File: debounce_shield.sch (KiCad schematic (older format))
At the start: 54 parts, among them J1 Conn_01x06, J2 RPi_GPIO, J3 Conn_01x06, J4 Conn_01x06, J5 Conn_01x02, P2 CONN_2, U1 74LV14D, U2 CAT24C32, U3 LTV-824, U4 LTV-824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

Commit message: Change 6-position terminal to fixed Phoenix Contact 1990041 footprint.
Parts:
- J1, J3, J4: footprint GSL002C-2.50-06P:GSL002C25006P -> Phoenix_Contact_1990041:1990041
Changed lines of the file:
@@
 F 0 "J4" H 1500 5450 50  0000 C CNN
 F 1 "Conn_01x06" H 1500 5350 50  0000 C CNN
-F 2 "GSL002C-2.50-06P:GSL002C25006P" H 1500 5050 50  0001 C CNN
+F 2 "Phoenix_Contact_1990041:1990041" H 1500 5050 50  0001 C CNN
 F 3 "~" H 1500 5050 50  0001 C CNN
 F 4 "Phoenix Contact" H 1500 5050 50  0001 C CNN "Manufacturer_Name"
@@
 F 0 "J3" H 1418 3875 50  0000 C CNN
 F 1 "Conn_01x06" H 1418 3966 50  0000 C CNN
-F 2 "GSL002C-2.50-06P:GSL002C25006P" H 1500 4400 50  0001 C CNN
+F 2 "Phoenix_Contact_1990041:1990041" H 1500 4400 50  0001 C CNN
 F 3 "~" H 1500 4400 50  0001 C CNN
 F 4 "Phoenix Contact" H 1500 4400 50  0001 C CNN "Manufacturer_Name"
@@
 F 0 "J1" H 4018 1175 50  0000 C CNN
 F 1 "Conn_01x06" H 4018 1266 50  0000 C CNN
-F 2 "GSL002C-2.50-06P:GSL002C25006P" H 4100 1700 50  0001 C CNN
+F 2 "Phoenix_Contact_1990041:1990041" H 4100 1700 50  0001 C CNN
 F 3 "~" H 4100 1700 50  0001 C CNN
 F 4 "Phoenix Contact" H 4100 1700 50  0001 C CNN "Manufacturer_Name"

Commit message: Update to v1.2-beta PCB revision.
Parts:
- removed C10: 100 nF, Capacitor_SMD:C_0603_1608Metric, symbol Device:C_Small
- removed D1: LM66100DCKR, LM66100DCKR:SOP65P210X110-6N, symbol LM66100DCKR:LM66100DCKR
- removed E1, E10, E11, E12, E13, E14, E2, E3, E4, E5, E6, E7, E8, E9: SPARK_GAP, libs:SG1210, symbol Device:SPARK_GAP
- removed P2: CONN_2, TerminalBlock_Phoenix:TerminalBlock_Phoenix_MPT-0,5-2-2.54_1x02_P2.54mm_Horizontal, symbol debounce_shield-rescue:CONN_2-debounce_shield-rescue
- removed R4: 1.2k, Resistor_SMD:R_1206_3216Metric_Pad1.42x1.75mm_HandSolder, symbol Device:R_Small
- removed RN1, RN2, RN3: YC164-JR-07100RL, YC164-JR-07100RL:YC164JR07220RL, symbol YC164-JR-07100RL:YC164-JR-07100RL
- removed U3, U4, U5: LTV-824, Package_DIP:DIP-8_W7.62mm, symbol Isolator:LTV-824
- added C7: 100 nF, Capacitor_SMD:C_0603_1608Metric, symbol debounce_shield-rescue:C-debounce_shield-rescue
- added C9: 10uF, Capacitor_SMD:C_1206_3216Metric, symbol Device:C_Small
- added D1, D2, D3, D4, D5, D6: D_TVS, Diode_SMD:D_SOD-123, symbol Device:D_TVS
- added D7: D_TVS, Diode_SMD:D_SMB, symbol Device:D_TVS
- added IC1, IC2, IC3, IC4, IC5, IC6: LTV-814, Package_DIP:DIP-4_W7.62mm, symbol LTV814:LTV-814
- added IC7: MAX16914AUB+, MAX16914AUB+:SOP50P490X110-10N, symbol MAX16914AUB+:MAX16914AUB+
- added J6: 1985218, Phoenix_Contact_1985218:1985218, symbol Connector_Generic:Conn_01x04
- added J7: 1285, Keystone_1285:1285, symbol 1285:1285
- added OVP1: LED, LED_SMD:LED_0805_2012Metric, symbol Device:LED
- added Q1, Q2: DMP3028LFDE7, DMP2066UFDE7:U-DFN2020-6, symbol DMP3028LFDE7:DMP3028LFDE7
- added R11, R12, R13, R14, R15, R16: 1k, Resistor_SMD:R_1206_3216Metric_Pad1.42x1.75mm_HandSolder, symbol Device:R_Small
- added R5, R6, R7: 1k, Resistor_SMD:R_0603_1608Metric, symbol Device:R_Small
- added R8: 3.9k, Resistor_SMD:R_0603_1608Metric, symbol Device:R_Small
- added RN1, RN2, RN3: R_Pack04, Resistor_SMD:R_Array_Convex_4x0603, symbol Device:R_Pack04
- C1: renamed from C6; value 100n -> 100 nF
- C12: renamed from C8; value 100n -> 100 nF
- C13: renamed from C7; value 100n -> 100 nF
- C2: renamed from C5; value 100n -> 100 nF
- C3: renamed from C4; value 100n -> 100 nF
- C4: renamed from C3; value 100n -> 100 nF
- C5: renamed from C2; value 100n -> 100 nF
- C6: renamed from C1; value 100n -> 100 nF
- R1: value 10k 1% -> 3.9k; Manufacturer_Part_Number RC0603FR-0710KL -> AC0603FR-133K9L; Mouser Part Number 603-RC0603FR-0710KL -> 603-AC0603FR-133K9L
- R21: renamed from R27; value 1.2k -> 1k
- R22: renamed from R26; value 1.2k -> 1k
- R23: renamed from R25; value 1.2k -> 1k
- R24: value 1.2k -> 1k
- R25: renamed from R23; value 1.2k -> 1k
- R26: renamed from R22; value 1.2k -> 1k
- renumbered C9 to C11, R20 to R2, R21 to R3, R19 to R4
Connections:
- wire segments 317 -> 351
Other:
- note added: "YC164-JR-0747KL"
- moved on the sheet: C11, C12, C13, H1, J1, J3, J4, J5, L1, PS1, PWR1, R2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

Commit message: Update the 74LV14D component.
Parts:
- U1: Manufacturer_Part_Number 74LV14D,112 -> 74LV14D,118; Mouser Part Number 771-LV14D112 -> 771-74LV14D-T
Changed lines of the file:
@@
 F 2 "Package_SO:SOIC-14_3.9x8.7mm_P1.27mm" H 6600 3450 60  0001 C CNN
 F 3 "https://assets.nexperia.com/documents/data-sheet/74LV14.pdf" H 6600 3450 60  0001 C CNN
-F 4 "771-LV14D112 " H 6600 3450 50  0001 C CNN "Mouser Part Number"
+F 4 "771-74LV14D-T " H 6600 3450 50  0001 C CNN "Mouser Part Number"
 F 5 "Nexperia" H 6600 3450 50  0001 C CNN "Manufacturer_Name"
-F 6 "74LV14D,112 " H 6600 3450 50  0001 C CNN "Manufacturer_Part_Number"
+F 6 "74LV14D,118 " H 6600 3450 50  0001 C CNN "Manufacturer_Part_Number"
 	1    6600 3450
 	1    0    0    -1
@@
 F 2 "Package_SO:SOIC-14_3.9x8.7mm_P1.27mm" H 6600 4350 60  0001 C CNN
 F 3 "https://assets.nexperia.com/documents/data-sheet/74LV14.pdf" H 6600 4350 60  0001 C CNN
-F 4 "771-LV14D112 " H 6600 4350 50  0001 C CNN "Mouser Part Number"
+F 4 "771-74LV14D-T " H 6600 4350 50  0001 C CNN "Mouser Part Number"
 F 5 "Nexperia" H 6600 4350 50  0001 C CNN "Manufacturer_Name"
-F 6 "74LV14D,112 " H 6600 4350 50  0001 C CNN "Manufacturer_Part_Number"
+F 6 "74LV14D,118 " H 6600 4350 50  0001 C CNN "Manufacturer_Part_Number"
 	2    6600 4350
 	1    0    0    -1
@@
 F 2 "Package_SO:SOIC-14_3.9x8.7mm_P1.27mm" H 6600 5700 60  0001 C CNN
 F 3 "https://assets.nexperia.com/documents/data-sheet/74LV14.pdf" H 6600 5700 60  0001 C CNN
-F 4 "771-LV14D112 " H 6600 5700 50  0001 C CNN "Mouser Part Number"
+F 4 "771-74LV14D-T " H 6600 5700 50  0001 C CNN "Mouser Part Number"
 F 5 "Nexperia" H 6600 5700 50  0001 C CNN "Manufacturer_Name"
-F 6 "74LV14D,112 " H 6600 5700 50  0001 C CNN "Manufacturer_Part_Number"
+F 6 "74LV14D,118 " H 6600 5700 50  0001 C CNN "Manufacturer_Part_Number"
 	3    6600 5700
 	1    0    0    -1
@@
 F 2 "Package_SO:SOIC-14_3.9x8.7mm_P1.27mm" H 6600 4800 60  0001 C CNN
 F 3 "https://assets.nexperia.com/documents/data-sheet/74LV14.pdf" H 6600 4800 60  0001 C CNN
-F 4 "771-LV14D112 " H 6600 4800 50  0001 C CNN "Mouser Part Number"
+F 4 "771-74LV14D-T " H 6600 4800 50  0001 C CNN "Mouser Part Number"
 F 5 "Nexperia" H 6600 4800 50  0001 C CNN "Manufacturer_Name"
-F 6 "74LV14D,112 " H 6600 4800 50  0001 C CNN "Manufacturer_Part_Number"
+F 6 "74LV14D,118 " H 6600 4800 50  0001 C CNN "Manufacturer_Part_Number"
 	5    6600 4800
 	1    0    0    -1
@@
 F 2 "Package_SO:SOIC-14_3.9x8.7mm_P1.27mm" H 6600 3900 60  0001 C CNN
 F 3 "https://assets.nexperia.com/documents/data-sheet/74LV14.pdf" H 6600 3900 60  0001 C CNN
-F 4 "771-LV14D112 " H 6600 3900 50  0001 C CNN "Mouser Part Number"
+F 4 "771-74LV14D-T " H 6600 3900 50  0001 C CNN "Mouser Part Number"
 F 5 "Nexperia" H 6600 3900 50  0001 C CNN "Manufacturer_Name"
-F 6 "74LV14D,112 " H 6600 3900 50  0001 C CNN "Manufacturer_Part_Number"
+F 6 "74LV14D,118 " H 6600 3900 50  0001 C CNN "Manufacturer_Part_Number"
 	6    6600 3900
 	1    0    0    -1
@@
 F 2 "Package_SO:SOIC-14_3.9x8.7mm_P1.27mm" H 6600 5250 60  0001 C CNN
 F 3 "https://assets.nexperia.com/documents/data-sheet/74LV14.pdf" H 6600 5250 60  0001 C CNN
-F 4 "771-LV14D112 " H 6600 5250 50  0001 C CNN "Mouser Part Number"
+F 4 "771-74LV14D-T " H 6600 5250 50  0001 C CNN "Mouser Part Number"
 F 5 "Nexperia" H 6600 5250 50  0001 C CNN "Manufacturer_Name"
-F 6 "74LV14D,112 " H 6600 5250 50  0001 C CNN "Manufacturer_Part_Number"
+F 6 "74LV14D,118 " H 6600 5250 50  0001 C CNN "Manufacturer_Part_Number"
 	4    6600 5250
 	1    0    0    -1

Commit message: Update to revision 1.3.
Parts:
- renumbered RN3 to RN12, RN2 to RN34, RN1 to RN56
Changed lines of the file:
@@
 EESchema Schematic File Version 4
 LIBS:debounce_shield-cache
-EELAYER 30 0
+EELAYER 29 0
 EELAYER END
 $Descr A4 11693 8268
@@
 $EndComp
 $Comp
-L Device:R_Pack04 RN1
+L Device:R_Pack04 RN56
 U 1 1 5E097139
 P 4550 3700
-F 0 "RN1" V 4875 3700 50  0000 C CNN
+F 0 "RN56" V 4875 3700 50  0000 C CNN
 F 1 "R_Pack04" V 4784 3700 50  0000 C CNN
 F 2 "Resistor_SMD:R_Array_Convex_4x0603" V 4825 3700 50  0001 C CNN
@@
 Text Notes 4050 3300 0    50   ~ 0
 YC164-JR-0747KL
-$Comp
-L Device:R_Pack04 RN2
-U 1 1 5E09E7B2
-P 4550 4600
-F 0 "RN2" V 4875 4600 50  0000 C CNN
-F 1 "R_Pack04" V 4784 4600 50  0000 C CNN
-F 2 "Resistor_SMD:R_Array_Convex_4x0603" V 4825 4600 50  0001 C CNN
-F 3 "https://eu.mouser.com/datasheet/2/447/PYu-YC_TC_group_51_RoHS_L_7-1313905.pdf" H 4550 4600 50  0001 C CNN
-F 4 "YAGEO - Resistor Networks & Arrays 47K Ohm 5% 1/16W 50 Volts " H 4550 4600 50  0001 C CNN "Description"
-F 5 "YAGEO (PHYCOMP)" H 4550 4600 50  0001 C CNN "Manufacturer_Name"
-F 6 "YC164-JR-0747KL " H 4550 4600 50  0001 C CNN "Manufacturer_Part_Number"
-F 7 "603-YC164-JR-0747KL " H 4550 4600 50  0001 C CNN "Mouser Part Number"
-F 8 "https://www.mouser.com/Search/Refine.aspx?Keyword=603-YC164-JR-07100RL" H 4550 4600 50  0001 C CNN "Mouser Price/Stock"
-	1    4550 4600
-	0    1    -1   0
-$EndComp
-$Comp
-L Device:R_Pack04 RN3
-U 1 1 5E09F4B1
-P 4550 5500
-F 0 "RN3" V 4875 5500 50  0000 C CNN
-F 1 "R_Pack04" V 4784 5500 50  0000 C CNN
-F 2 "Resistor_SMD:R_Array_Convex_4x0603" V 4825 5500 50  0001 C CNN
-F 3 "https://eu.mouser.com/datasheet/2/447/PYu-YC_TC_group_51_RoHS_L_7-1313905.pdf" H 4550 5500 50  0001 C CNN
-F 4 "YAGEO - Resistor Networks & Arrays 47K Ohm 5% 1/16W 50 Volts " H 4550 5500 50  0001 C CNN "Description"
-F 5 "YAGEO (PHYCOMP)" H 4550 5500 50  0001 C CNN "Manufacturer_Name"
-F 6 "YC164-JR-0747KL " H 4550 5500 50  0001 C CNN "Manufacturer_Part_Number"
-F 7 "603-YC164-JR-0747KL " H 4550 5500 50  0001 C CNN "Mouser Part Number"
-F 8 "https://www.mouser.com/Search/Refine.aspx?Keyword=603-YC164-JR-07100RL" H 4550 5500 50  0001 C CNN "Mouser Price/Stock"
-	1    4550 5500
-	0    1    -1   0
-$EndComp
 Wire Wire Line
 	2600 4100 2650 4100
@@
 Wire Wire Line
 	2300 2350 2450 2350
+$Comp
+L Device:R_Pack04 RN34
+U 1 1 5E09E7B2
+P 4550 4600
+F 0 "RN34" V 4875 4600 50  0000 C CNN
+F 1 "R_Pack04" V 4784 4600 50  0000 C CNN
+F 2 "Resistor_SMD:R_Array_Convex_4x0603" V 4825 4600 50  0001 C CNN
+F 3 "https://eu.mouser.com/datasheet/2/447/PYu-YC_TC_group_51_RoHS_L_7-1313905.pdf" H 4550 4600 50  0001 C CNN
+F 4 "YAGEO - Resistor Networks & Arrays 47K Ohm 5% 1/16W 50 Volts " H 4550 4600 50  0001 C CNN "Description"
+F 5 "YAGEO (PHYCOMP)" H 4550 4600 50  0001 C CNN "Manufacturer_Name"
+F 6 "YC164-JR-0747KL " H 4550 4600 50  0001 C CNN "Manufacturer_Part_Number"
+F 7 "603-YC164-JR-0747KL " H 4550 4600 50  0001 C CNN "Mouser Part Number"
+F 8 "https://www.mouser.com/Search/Refine.aspx?Keyword=603-YC164-JR-07100RL" H 4550 4600 50  0001 C CNN "Mouser Price/Stock"
+	1    4550 4600
+	0    1    -1   0
+$EndComp
+$Comp
+L Device:R_Pack04 RN12
+U 1 1 5E09F4B1
+P 4550 5500
+F 0 "RN12" V 4875 5500 50  0000 C CNN
+F 1 "R_Pack04" V 4784 5500 50  0000 C CNN
+F 2 "Resistor_SMD:R_Array_Convex_4x0603" V 4825 5500 50  0001 C CNN
+F 3 "https://eu.mouser.com/datasheet/2/447/PYu-YC_TC_group_51_RoHS_L_7-1313905.pdf" H 4550 5500 50  0001 C CNN
+F 4 "YAGEO - Resistor Networks & Arrays 47K Ohm 5% 1/16W 50 Volts " H 4550 5500 50  0001 C CNN "Description"
+F 5 "YAGEO (PHYCOMP)" H 4550 5500 50  0001 C CNN "Manufacturer_Name"
+F 6 "YC164-JR-0747KL " H 4550 5500 50  0001 C CNN "Manufacturer_Part_Number"
+F 7 "603-YC164-JR-0747KL " H 4550 5500 50  0001 C CNN "Mouser Part Number"
+F 8 "https://www.mouser.com/Search/Refine.aspx?Keyword=603-YC164-JR-07100RL" H 4550 5500 50  0001 C CNN "Mouser Price/Stock"
+	1    4550 5500
+	0    1    -1   0
+$EndComp
 $EndSCHEMATC

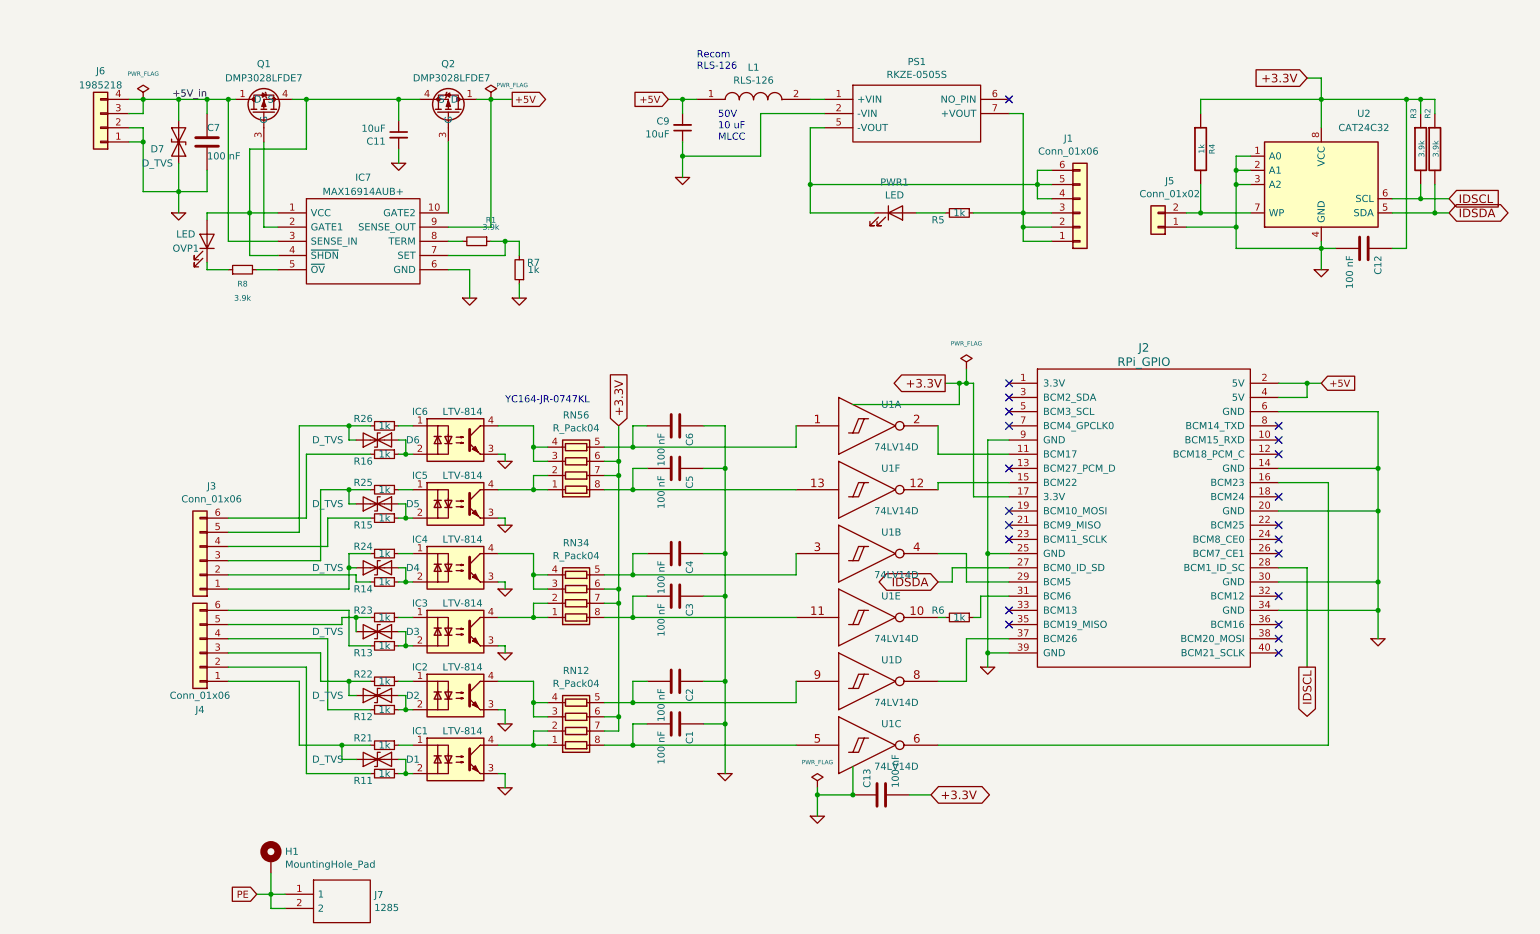
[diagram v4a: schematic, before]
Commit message: Add additional filtering and protection to DC-DC circuit.
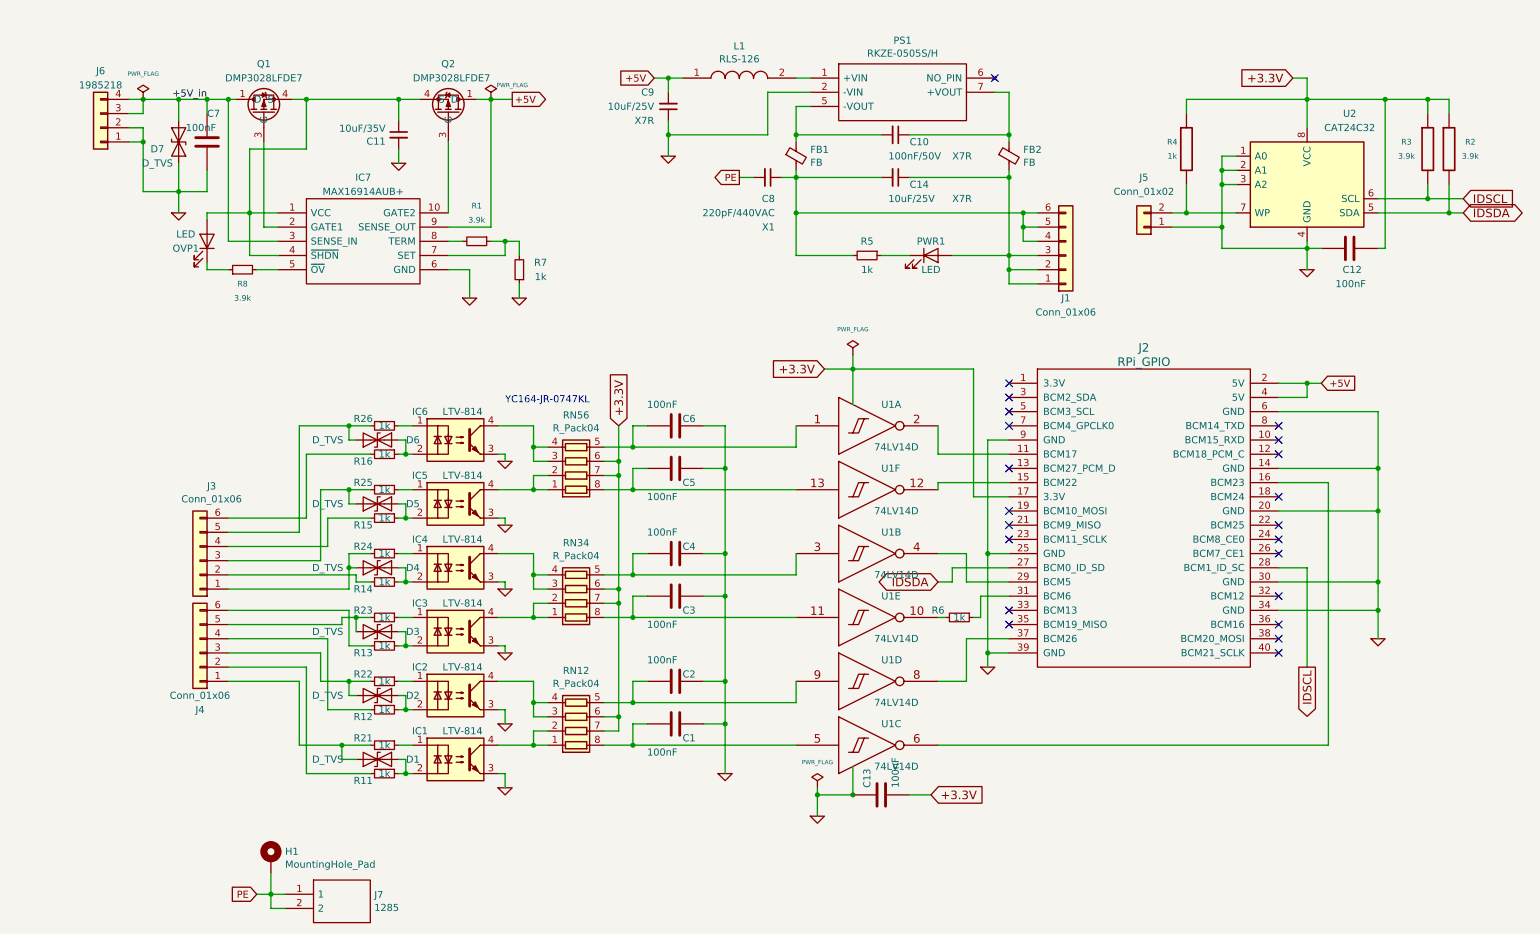
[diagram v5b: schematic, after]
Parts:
- added C10: 100nF/50V, Capacitor_SMD:C_0603_1608Metric, symbol Device:C_Small
- added C14: 10uF/25V, Capacitor_SMD:C_1206_3216Metric, symbol Device:C_Small
- added C8: 220pF/440VAC, Varistor:RV_Disc_D12mm_W4.6mm_P7.5mm, symbol Device:C_Small
- added FB1, FB2: FB, Inductor_SMD:L_0805_2012Metric, symbol Device:Ferrite_Bead_Small
- C1, C12, C13, C2, C3, C4, C5, C6, C7: value 100 nF -> 100nF; Manufacturer_Name Wurth Elektronik -> Taiyo Yuden; Manufacturer_Part_Number 885012206071 -> GMK107B7104KAHT; Mouser Part Number 710-885012206071 -> 963-GMK107B7104KAHT
- C11: value 10uF -> 10uF/35V; Manufacturer_Name Taiyo Yuden -> Taiyo Yuden; Manufacturer_Part_Number UMK316BBJ106ML-T -> GMK316AB7106KL-TR; Mouser Part Number 963-UMK316BBJ106ML-T -> 963-GMK316AB7106KL; Technology (none) -> X7R
- C9: value 10uF -> 10uF/25V; Manufacturer_Name Taiyo Yuden -> Taiyo Yuden; Manufacturer_Part_Number UMK316BBJ106ML-T -> TMK316B7106KL-TD; Mouser Part Number 963-UMK316BBJ106ML-T -> 963-TMK316B7106KL-TD; Technology (none) -> X7R
- H1: Manufacturer_Name (none) -> (none)
- PS1: value RKZE-0505S -> RKZE-0505S/H; Manufacturer_Part_Number RKZE-0505S -> RKZE-0505S/H; Mouser Part Number 919-RKZE-0505S -> 919-RKZE-0505S/H
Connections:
- net PE: now also C8.2
- net at J1.4 (Pin_4), J1.5 (Pin_5), J1.6 (Pin_6): now also R5.2, C14.2, C8.1, FB1.2; no longer PS1.5 (-VOUT), PWR1.1 (K)
- net at J1.1 (Pin_1), J1.2 (Pin_2), J1.3 (Pin_3): now also PWR1.2 (A), C14.1, FB2.2; no longer PS1.7 (+VOUT), R5.1
- new net: C10.2, FB1.1, PS1.5 (-VOUT)
- new net: C10.1, FB2.1, PS1.7 (+VOUT)
- new net: PWR1.1 (K), R5.1
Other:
- note removed: "50V\n10 uF\nMLCC"
- note removed: "Recom\nRLS-126"
- moved on the sheet: C12, C9, J1, J5, L1, PS1, PWR1, R2, R3, R4, R5, U2

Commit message: Add solder jumpers for EEPROM, additional artwork.
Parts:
- added JP1, JP2, JP3: SJ3_Bridged12, Jumper:SolderJumper-3_P1.3mm_Bridged12_RoundedPad1.0x1.5mm, symbol Jumper:SolderJumper_3_Bridged12
- H1: footprint MountingHole:MountingHole_3.5mm_Pad -> MountingHole:MountingHole_3.5mm_Pad_Via
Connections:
- net labels added: A0, A1, A2
- wire segments 361 -> 372
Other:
- moved on the sheet: C10, C11, C14, C7, C8, C9, D7, FB1, FB2, IC7, J1, J5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
